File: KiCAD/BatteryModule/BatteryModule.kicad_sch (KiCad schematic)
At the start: 8 parts

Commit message: 配線できました。確認お願いします。
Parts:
- removed J?: Conn_01x08, symbol Connector_Generic:Conn_01x08
- removed J?: Conn_01x04, symbol Connector_Generic:Conn_01x04
- Battery1: renamed from J?; footprint (none) -> TSRP_Connector_Hirose:DF1B-2S-2.5R
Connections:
- net at BT1.1 (+): now also Battery1.1 (Pin_1)
- net PowerModule: now reaches Battery1.2 (Pin_2)
- no-connect marks 0 -> 1
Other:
- moved on the sheet: Battery1
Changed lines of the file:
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@@
 	(generator_version "9.0")
 	(paper "A4")
+	(no_connect
+		(at 111.76 64.77)
+	)
 	(wire
 		(pts
@@
 			(width 0)
 			(type default)
+		)
+	)
+	(wire
+		(pts
+			(xy 88.9 64.77) (xy 111.76 64.77)
+		)
+		(stroke
+			(width 0)
+			(type default)
+		)
+	)
+	(label "PowerModule"
+		(at 99.06 64.77 0)
+		(effects
+			(font
+				(size 1.27 1.27)
+			)
+			(justify left bottom)
 		)
 	)
@@
 	)
 	(symbol
-		(lib_id "Connector_Generic:Conn_01x08")
-		(at 173.99 46.99 90)
-		(unit 1)
-		(exclude_from_sim no)
-		(in_bom yes)
-		(on_board yes)
-		(dnp no)
-		(fields_autoplaced yes)
-		(property "Reference" "J?"
-			(at 173.9899 44.45 0)
-			(effects
-				(font
-					(size 1.27 1.27)
-				)
-				(justify left)
-			)
-		)
-		(property "Value" "Conn_01x08"
-			(at 176.5299 44.45 0)
-			(effects
-				(font
-					(size 1.27 1.27)
-				)
-				(justify left)
-			)
-		)
-		(property "Footprint" ""
-			(at 173.99 46.99 0)
-			(effects
-				(font
-					(size 1.27 1.27)
-				)
-				(hide yes)
-			)
-		)
-		(property "Datasheet" "~"
-			(at 173.99 46.99 0)
-			(effects
-				(font
-					(size 1.27 1.27)
-				)
-				(hide yes)
-			)
-		)
-		(property "Description" "Generic connector, single row, 01x08, script generated (kicad-library-utils/schlib/autogen/connector/)"
-			(at 173.99 46.99 0)
-			(effects
-				(font
-					(size 1.27 1.27)
-				)
-				(hide yes)
-			)
-		)
-		(pin "8"
-		)
-		(pin "1"
-		)
-		(pin "2"
-		)
-		(pin "3"
-		)
-		(pin "4"
-		)
-		(pin "5"
-		)
-		(pin "6"
-		)
-		(pin "7"
-		)
-		(instances
-			(project ""
-				(path "/5fdab1fc-8753-4791-a1ef-316a96bc502f"
-					(reference "J?")
-					(unit 1)
-				)
-			)
-		)
-	)
-	(symbol
-		(lib_id "Connector_Generic:Conn_01x04")
-		(at 142.24 46.99 90)
-		(unit 1)
-		(exclude_from_sim no)
-		(in_bom yes)
-		(on_board yes)
-		(dnp no)
-		(fields_autoplaced yes)
-		(property "Reference" "J?"
-			(at 142.2399 44.45 0)
-			(effects
-				(font
-					(size 1.27 1.27)
-				)
-				(justify left)
-			)
-		)
-		(property "Value" "Conn_01x04"
-			(at 144.7799 44.45 0)
-			(effects
-				(font
-					(size 1.27 1.27)
-				)
-				(justify left)
-			)
-		)
-		(property "Footprint" ""
-			(at 142.24 46.99 0)
-			(effects
-				(font
-					(size 1.27 1.27)
-				)
-				(hide yes)
-			)
-		)
-		(property "Datasheet" "~"
-			(at 142.24 46.99 0)
-			(effects
-				(font
-					(size 1.27 1.27)
-				)
-				(hide yes)
-			)
-		)
-		(property "Description" "Generic connector, single row, 01x04, script generated (kicad-library-utils/schlib/autogen/connector/)"
-			(at 142.24 46.99 0)
-			(effects
-				(font
-					(size 1.27 1.27)
-				)
-				(hide yes)
-			)
-		)
-		(pin "2"
-		)
-		(pin "1"
-		)
-		(pin "3"
-		)
-		(pin "4"
-		)
-		(instances
-			(project ""
-				(path "/5fdab1fc-8753-4791-a1ef-316a96bc502f"
-					(reference "J?")
-					(unit 1)
-				)
-			)
-		)
-	)
-	(symbol
 		(lib_id "Device:Battery_Cell")
 		(at 86.36 110.49 0)
@@
 	(symbol
 		(lib_id "Connector_Generic:Conn_01x02")
-		(at 156.21 46.99 90)
-		(unit 1)
-		(exclude_from_sim no)
-		(in_bom yes)
-		(on_board yes)
-		(dnp no)
-		(fields_autoplaced yes)
-		(property "Reference" "J?"
-			(at 156.2099 44.45 0)
+		(at 86.36 59.69 90)
+		(unit 1)
+		(exclude_from_sim no)
+		(in_bom yes)
+		(on_board yes)
+		(dnp no)
+		(fields_autoplaced yes)
+		(property "Reference" "Battery1"
+			(at 86.3599 57.15 0)
 			(effects
 				(font
@@
 		)
 		(property "Value" "Conn_01x02"
-			(at 158.7499 44.45 0)
-			(effects
-				(font
-					(size 1.27 1.27)
-				)
-				(justify left)
-			)
-		)
-		(property "Footprint" ""
-			(at 156.21 46.99 0)
+			(at 88.8999 57.15 0)
+			(effects
+				(font
+					(size 1.27 1.27)
+				)
+				(justify left)
+			)
+		)
+		(property "Footprint" "TSRP_Connector_Hirose:DF1B-2S-2.5R"
+			(at 86.36 59.69 0)
 			(effects
 				(font
@@
 		)
 		(property "Datasheet" "~"
-			(at 156.21 46.99 0)
+			(at 86.36 59.69 0)
 			(effects
 				(font
@@
 		)
 		(property "Description" "Generic connector, single row, 01x02, script generated (kicad-library-utils/schlib/autogen/connector/)"
-			(at 156.21 46.99 0)
+			(at 86.36 59.69 0)
 			(effects
 				(font
@@
 			(project ""
 				(path "/5fdab1fc-8753-4791-a1ef-316a96bc502f"
-					(reference "J?")
-					(unit 1)
-				)
+					(reference "Battery1")
+					(unit 1)
+				)

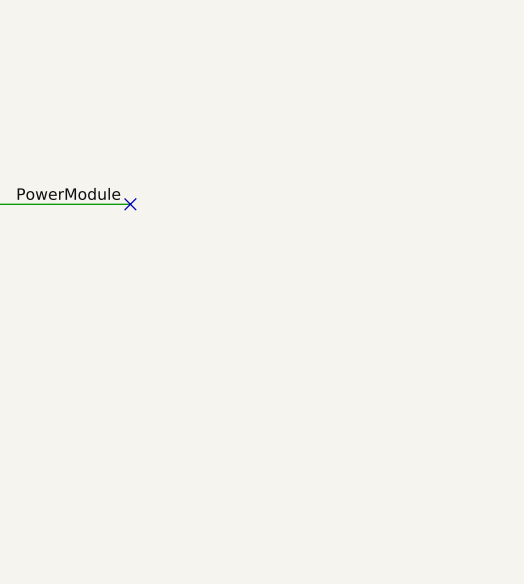
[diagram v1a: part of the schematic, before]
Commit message: BatteryModuleの外形完成
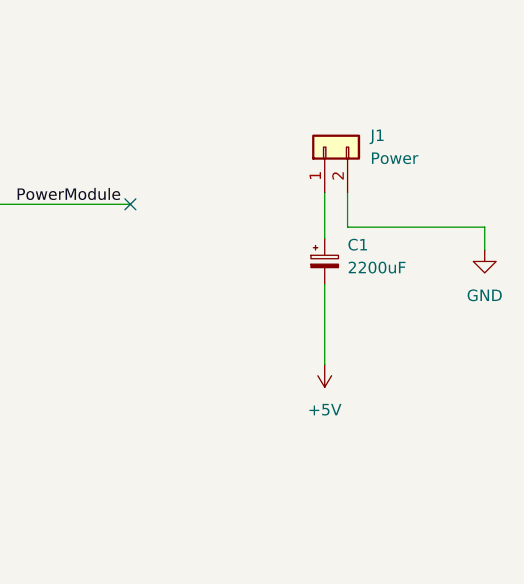
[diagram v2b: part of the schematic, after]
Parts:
- added C1: 2200uF, Capacitor_THT:CP_Radial_D18.0mm_P7.50mm, symbol Device:C_Polarized_Small
- added J1: Power, TSRP_Connector_Hirose:DF1B-2S-2.5R, symbol Connector_Generic:Conn_01x02
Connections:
- net GND: now also J1.2 (Pin_2)
- new net: C1.1, J1.1 (Pin_1)
- new net +5V: C1.2

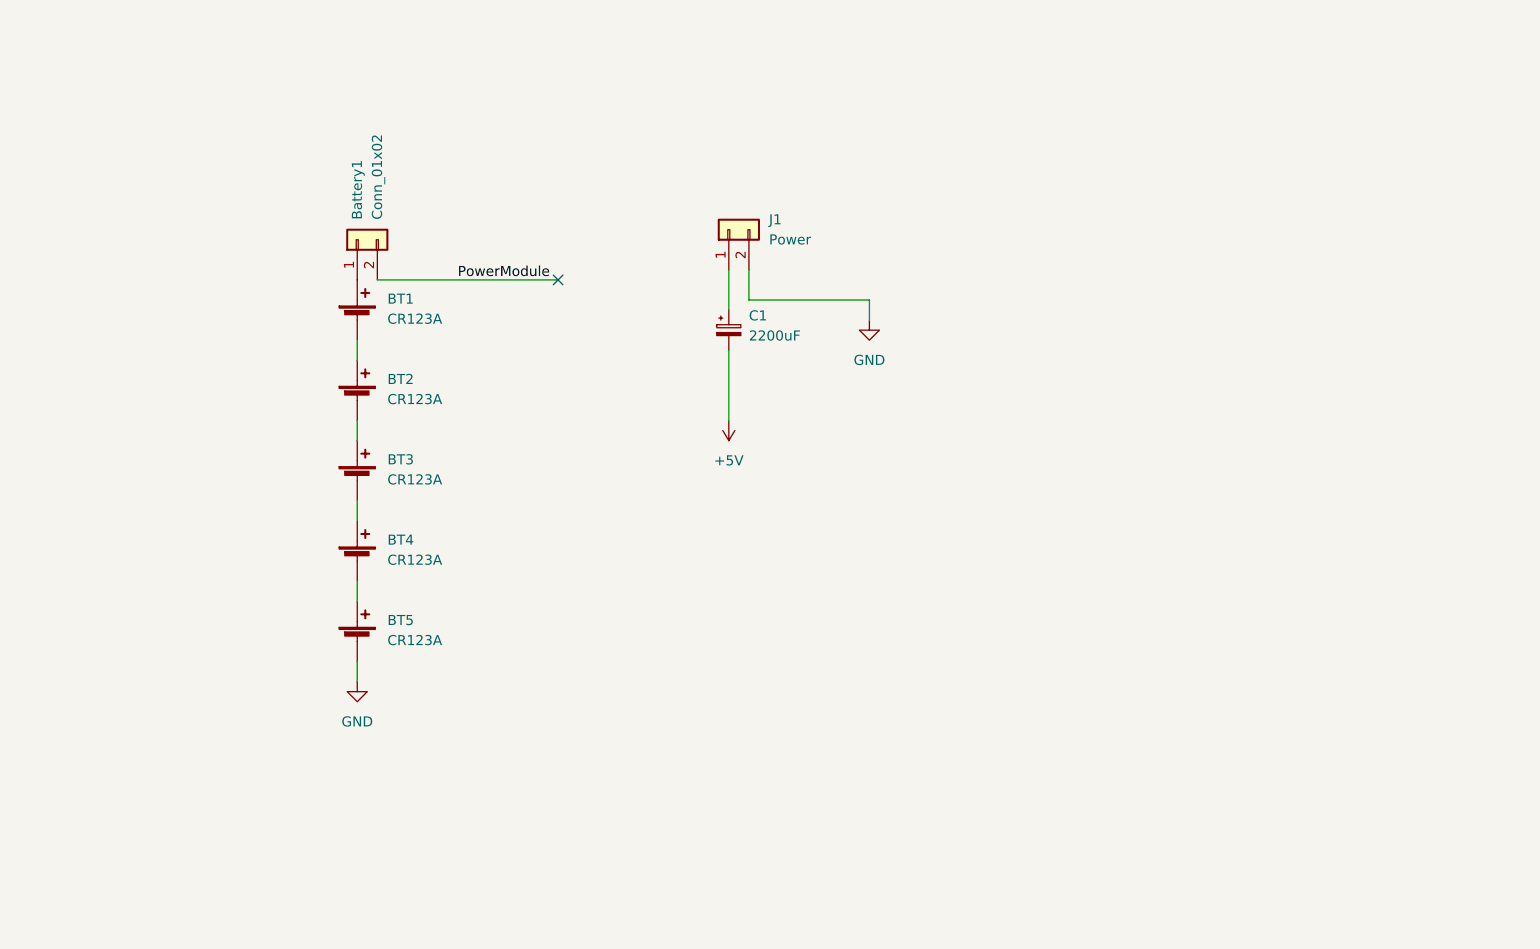
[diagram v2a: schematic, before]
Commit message: 取付穴位置を変更．キャパシターをSubaru Plateへ移動
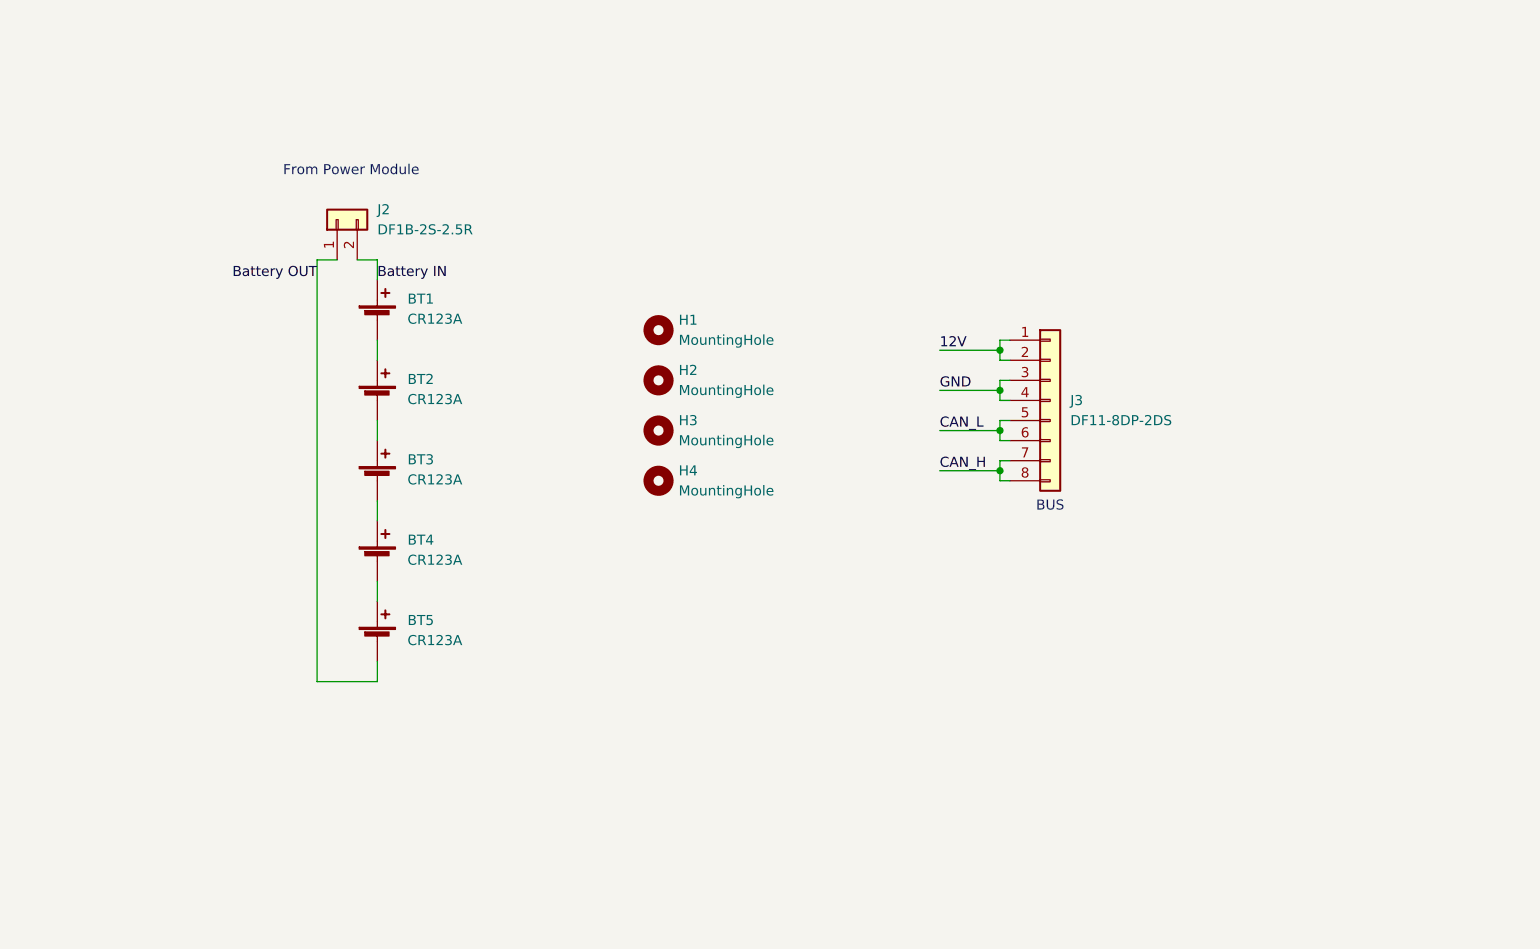
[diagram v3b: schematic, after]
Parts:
- removed Battery1: Conn_01x02, TSRP_Connector_Hirose:DF1B-2S-2.5R, symbol Connector_Generic:Conn_01x02
- removed C1: 2200uF, Capacitor_THT:CP_Radial_D18.0mm_P7.50mm, symbol Device:C_Polarized_Small
- removed J1: Power, TSRP_Connector_Hirose:DF1B-2S-2.5R, symbol Connector_Generic:Conn_01x02
- added H1, H2, H3, H4: MountingHole, MountingHole:MountingHole_3.2mm_M3_Pad_TopBottom, symbol Mechanical:MountingHole
- added J2: DF1B-2S-2.5R, TSRP_Connector_Hirose:DF1B-2S-2.5R, symbol Connector_Generic:Conn_01x02
- added J3: DF11-8DP-2DS, TSRP_Connector_Hirose:DF11-8DP-2DS, symbol Connector_Generic:Conn_01x08
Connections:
- net GND: now also J3.3 (Pin_3), J3.4 (Pin_4); no longer BT5.2 (-)
- net Battery IN: now reaches BT1.1 (+)
- net Battery IN: now also J2.2 (Pin_2)
- new net 12V: J3.1 (Pin_1), J3.2 (Pin_2)
- new net Battery OUT: BT5.2 (-), J2.1 (Pin_1)
- new net CAN_H: J3.7 (Pin_7), J3.8 (Pin_8)
- new net CAN_L: J3.5 (Pin_5), J3.6 (Pin_6)
- no-connect marks 1 -> 0
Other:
- note added: "BUS"
- note added: "From Power Module"
- moved on the sheet: BT1, BT2, BT3, BT4, BT5

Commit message: 3Dモデルを組み合わせて結合試験する．
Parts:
- added D1: Green, LED_SMD:LED_0603_1608Metric_Pad1.05x0.95mm_HandSolder, symbol Device:LED_Small
- added R1: 2.4kR, Resistor_SMD:R_0603_1608Metric_Pad0.98x0.95mm_HandSolder, symbol Device:R
- added TP1, TP2: TestPoint, TestPoint:TestPoint_THTPad_D2.0mm_Drill1.0mm, symbol Connector:TestPoint
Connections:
- net 12V: now also R1.1
- net Battery IN: now also TP1.1
- net Battery OUT: now also TP2.1
- net GND: now also D1.1 (K)
- new net: D1.2 (A), R1.2
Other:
- moved on the sheet: BT1, BT2, BT3, BT4, BT5, H1, H2, H3, H4, J2, J3

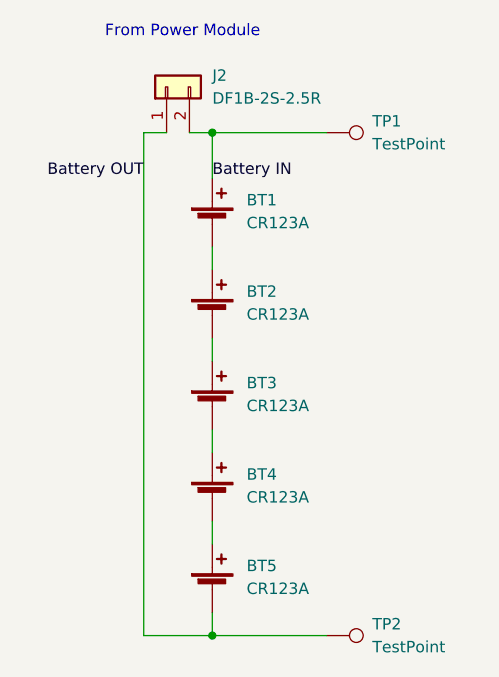
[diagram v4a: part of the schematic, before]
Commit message: 3Dモデルを組み合わせて結合試験する
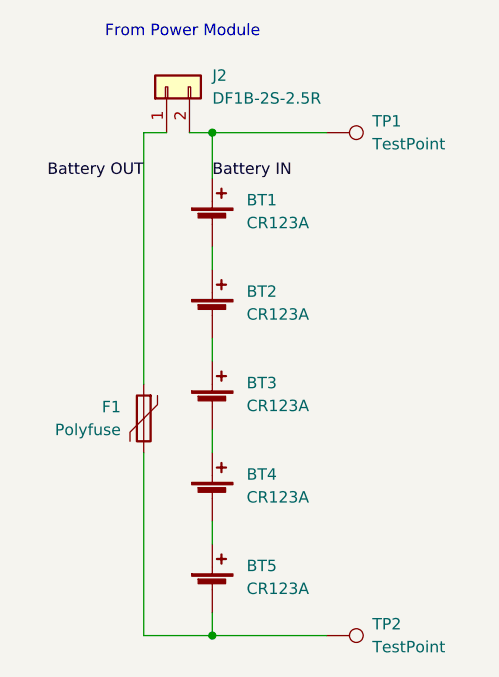
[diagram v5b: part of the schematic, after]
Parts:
- added F1: Polyfuse, Fuse:Fuse_Bourns_MF-RHT300, symbol Device:Polyfuse
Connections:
- net Battery OUT: now also F1.1; no longer BT5.2 (-), TP2.1
- new net: BT5.2 (-), F1.2, TP2.1
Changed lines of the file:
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@@
+	(wire
+		(pts
+			(xy 57.15 96.52) (xy 57.15 116.84)
+		)
+		(stroke
+			(width 0)
+			(type default)
+		)
+	)
 	(wire
 		(pts
@@
 	(wire
 		(pts
-			(xy 57.15 116.84) (xy 57.15 60.96)
-		)
-		(stroke
-			(width 0)
-			(type default)
-		)
-	)
-	(wire
-		(pts
 			(xy 190.5 83.82) (xy 190.5 85.09)
 		)
@@
 		(pts
 			(xy 190.5 87.63) (xy 190.5 88.9)
+		)
+		(stroke
+			(width 0)
+			(type default)
+		)
+	)
+	(wire
+		(pts
+			(xy 57.15 60.96) (xy 57.15 88.9)
 		)
 		(stroke
@@
 					(unit 1)
 				)
+			)
+		)
+	)
+	(symbol
+		(lib_id "Device:Polyfuse")
+		(at 57.15 92.71 0)
+		(mirror y)
+		(unit 1)
+		(exclude_from_sim no)
+		(in_bom yes)
+		(on_board yes)
+		(dnp no)
+		(property "Reference" "F1"
+			(at 54.61 91.4399 0)
+			(effects
+				(font
+					(size 1.27 1.27)
+				)
+				(justify left)
+			)
+		)
+		(property "Value" "Polyfuse"
+			(at 54.61 93.9799 0)
+			(effects
+				(font
+					(size 1.27 1.27)
+				)
+				(justify left)
+			)
+		)
+		(property "Footprint" "Fuse:Fuse_Bourns_MF-RHT300"
+			(at 55.88 97.79 0)
+			(effects
+				(font
+					(size 1.27 1.27)
+				)
+				(justify left)
+				(hide yes)
+			)
+		)
+		(property "Datasheet" "~"
+			(at 57.15 92.71 0)
+			(effects
+				(font
+					(size 1.27 1.27)
+				)
+				(hide yes)
+			)
+		)
+		(property "Description" "Resettable fuse, polymeric positive temperature coefficient"
+			(at 57.15 92.71 0)
+			(effects
+				(font
+					(size 1.27 1.27)
+				)
+				(hide yes)
+			)
+		)
+		(pin "2"
+		)
+		(pin "1"
+		)
+		(instances
+			(project ""
+				(path "/5fdab1fc-8753-4791-a1ef-316a96bc502f"
+					(reference "F1")
+					(unit 1)
+				)

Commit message: BatteryModule，Build-2完成．今日発注
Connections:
- net Battery IN: now also F1.1; no longer BT1.1 (+)
- net GND: now also BT5.2 (-), J2.1 (Pin_1), TP2.1; no longer D1.1 (K), J3.3 (Pin_3), J3.4 (Pin_4)
- removed net Battery OUT: F1.1, J2.1 (Pin_1)
- new net: BT1.1 (+), F1.2
- new net BUS_GND: D1.1 (K), J3.3 (Pin_3), J3.4 (Pin_4)
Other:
- moved on the sheet: BT1, BT2, BT3, BT4, BT5, F1, J3, TP2
